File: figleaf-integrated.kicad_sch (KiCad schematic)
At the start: 63 parts, among them J1 UDB, J2 HRO_TYPE-C-31-M-14, J3 Battery, J9 TC2030_SWD, Q2 2N7002, SW1 PWR, SW2 RST, U1 SRV05-4, U10 MAX17048, U3 BQ24075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

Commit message: progress + add jst conn
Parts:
- J3: footprint PCM_marbastlib-various:Molex_Pico-EZmate_78171-0002_1x02-1MP_P1.20mm_Vertical -> Connector_JST:JST_SH_SM02B-SRSS-TB_1x02-1MP_P1.00mm_Horizontal
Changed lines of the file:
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@@
 			)
 		)
-		(property "Footprint" "PCM_marbastlib-various:Molex_Pico-EZmate_78171-0002_1x02-1MP_P1.20mm_Vertical"
+		(property "Footprint" "Connector_JST:JST_SH_SM02B-SRSS-TB_1x02-1MP_P1.00mm_Horizontal"
 			(at 236.22 57.15 0)
 			(effects

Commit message: Add matrix
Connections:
- net col_5: now also U8.11 (P0.27); no longer U8.35 (P1.10-LF)
- net row_0: now also U8.16 (P0.08); no longer U8.36 (P1.11-LF)
- net row_1: now also U8.15 (P0.11); no longer U8.37 (P1.12-LF)
- net row_2: now also U8.14 (P0.06); no longer U8.38 (P1.13-LF)
- net row_3: now also U8.13 (P0.04-A); no longer U8.40 (P1.14-LF)
- net row_4: now also U8.12 (P0.26); no longer U8.41 (P1.15-LF)

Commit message: tracing progress
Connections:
- net GNDPWR is gone; now on net GND_L: R1.1, R2.1
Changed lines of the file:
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@@
 	)
 	(symbol
-		(lib_id "power:GNDPWR")
+		(lib_id "power:GND")
 		(at 67.31 41.91 0)
 		(unit 1)
@@
 			)
 		)
-		(property "Value" "GNDPWR"
+		(property "Value" "GND_L"
 			(at 67.4116 45.8216 0)
 			(effects
@@
 		)
 		(property "Footprint" ""
-			(at 67.31 43.18 0)
+			(at 67.31 41.91 0)
 			(effects
 				(font
@@
 		)
 		(property "Datasheet" ""
-			(at 67.31 43.18 0)
+			(at 67.31 41.91 0)
 			(effects
 				(font
@@
 			)
 		)
-		(property "Description" "Power symbol creates a global label with name \"GNDPWR\" , global ground"
+		(property "Description" "Power symbol creates a global label with name \"GND\" , ground"
 			(at 67.31 41.91 0)
 			(effects

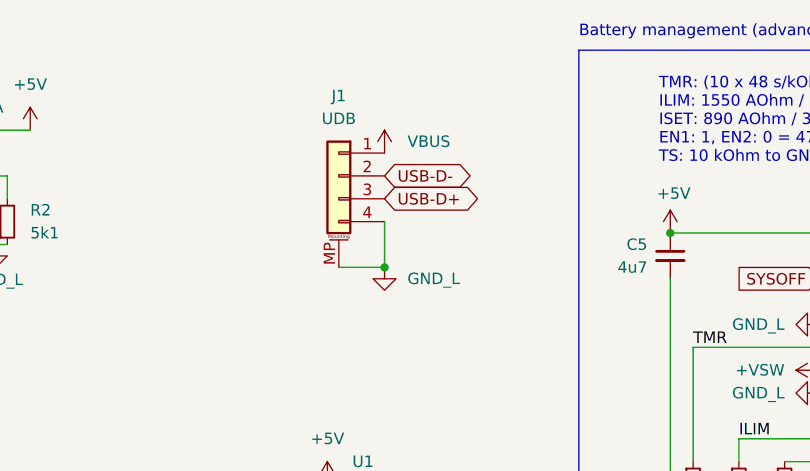
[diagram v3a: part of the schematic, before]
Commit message: remove J4 connector, not using DB board
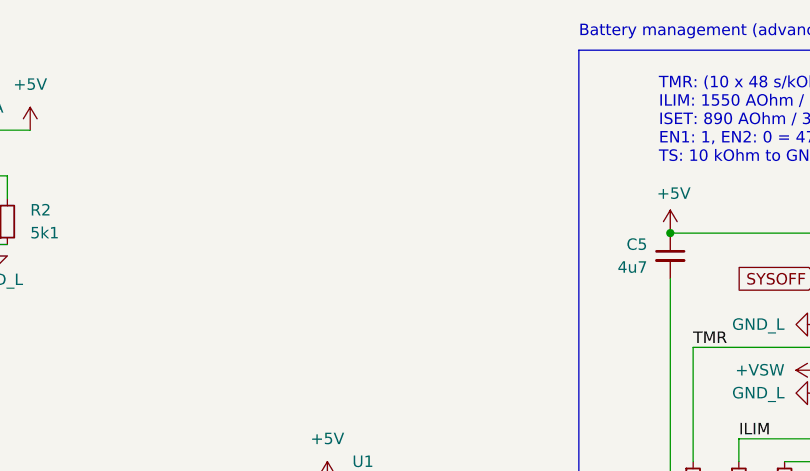
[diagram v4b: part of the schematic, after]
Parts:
- removed J1: UDB, symbol Connector_Generic_MountingPin:Conn_01x04_MountingPin

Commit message: pcb progress
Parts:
- U10: footprint Package_DFN_QFN:DFN-8-1EP_2x2mm_P0.5mm_EP0.7x1.3mm -> Graz_Footprints:DFN-8-1EP_2x2mm_P0.5mm_EP0.7x1.3mm
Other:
- moved on the sheet: U1
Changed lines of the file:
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@@
 	)
 	(no_connect
-		(at 116.84 78.74)
+		(at 116.84 43.18)
 	)
 	(no_connect
@@
 	)
 	(no_connect
-		(at 91.44 83.82)
+		(at 91.44 48.26)
 	)
 	(no_connect
@@
 	(global_label "USB-D-"
 		(shape bidirectional)
-		(at 91.44 78.74 180)
+		(at 91.44 43.18 180)
 		(fields_autoplaced yes)
 		(effects
@@
 		)
 		(property "Intersheetrefs" "${INTERSHEET_REFS}"
-			(at 79.1981 78.74 0)
+			(at 79.1981 43.18 0)
 			(effects
 				(font
@@
 	(global_label "USB-D+"
 		(shape bidirectional)
-		(at 116.84 83.82 0)
+		(at 116.84 48.26 0)
 		(fields_autoplaced yes)
 		(effects
@@
 		)
 		(property "Intersheetrefs" "${INTERSHEET_REFS}"
-			(at 129.0819 83.82 0)
+			(at 129.0819 48.26 0)
 			(effects
 				(font
@@
 	(symbol
 		(lib_id "power:GND")
-		(at 104.14 93.98 0)
+		(at 104.14 58.42 0)
 		(unit 1)
 		(exclude_from_sim no)
@@
 		(dnp no)
 		(property "Reference" "#PWR09"
-			(at 104.14 100.33 0)
+			(at 104.14 64.77 0)
 			(effects
 				(font
@@
 		)
 		(property "Value" "GND_L"
-			(at 104.267 98.3742 0)
+			(at 104.267 62.8142 0)
 			(effects
 				(font
@@
 		)
 		(property "Footprint" ""
-			(at 104.14 93.98 0)
+			(at 104.14 58.42 0)
 			(effects
 				(font
@@
 		)
 		(property "Datasheet" ""
-			(at 104.14 93.98 0)
+			(at 104.14 58.42 0)
 			(effects
 				(font
@@
 		)
 		(property "Description" "Power symbol creates a global label with name \"GND\" , ground"
-			(at 104.14 93.98 0)
+			(at 104.14 58.42 0)
 			(effects
 				(font
@@
 			)
 		)
-		(property "Footprint" "Package_DFN_QFN:DFN-8-1EP_2x2mm_P0.5mm_EP0.7x1.3mm"
+		(property "Footprint" "Graz_Footprints:DFN-8-1EP_2x2mm_P0.5mm_EP0.7x1.3mm"
 			(at 153.035 138.43 0)
 			(effects
@@
 	(symbol
 		(lib_id "Power_Protection:SRV05-4")
-		(at 104.14 81.28 0)
+		(at 104.14 45.72 0)
 		(unit 1)
 		(exclude_from_sim no)
@@
 		(fields_autoplaced yes)
 		(property "Reference" "U1"
-			(at 106.9087 66.04 0)
+			(at 106.9087 30.48 0)
 			(effects
 				(font
@@
 		)
 		(property "Value" "SRV05-4"
-			(at 106.9087 68.58 0)
+			(at 106.9087 33.02 0)
 			(effects
 				(font
@@
 		)
 		(property "Footprint" "Package_TO_SOT_SMD:SOT-23-6"
-			(at 121.92 92.71 0)
+			(at 121.92 57.15 0)
 			(effects
 				(font
@@
 		)
 		(property "Datasheet" "http://www.onsemi.com/pub/Collateral/SRV05-4-D.PDF"
-			(at 104.14 81.28 0)
+			(at 104.14 45.72 0)
 			(effects
 				(font
@@
 		)
 		(property "Description" "ESD Protection Diodes with Low Clamping Voltage, SOT-23-6"
-			(at 104.14 81.28 0)
+			(at 104.14 45.72 0)
 			(effects
 				(font
@@
 	(symbol
 		(lib_id "power:+5V")
-		(at 104.14 68.58 0)
+		(at 104.14 33.02 0)
 		(unit 1)
 		(exclude_from_sim no)
@@
 		(fields_autoplaced yes)
 		(property "Reference" "#PWR06"
-			(at 104.14 72.39 0)
+			(at 104.14 36.83 0)
 			(effects
 				(font
@@
 		)
 		(property "Value" "+5V"
-			(at 104.14 63.5 0)
+			(at 104.14 27.94 0)
 			(effects
 				(font
@@
 		)
 		(property "Footprint" ""
-			(at 104.14 68.58 0)
+			(at 104.14 33.02 0)
 			(effects
 				(font
@@
 		)
 		(property "Datasheet" ""
-			(at 104.14 68.58 0)
+			(at 104.14 33.02 0)
 			(effects
 				(font
@@
 		)
 		(property "Description" "Power symbol creates a global label with name \"+5V\""
-			(at 104.14 68.58 0)
+			(at 104.14 33.02 0)
 			(effects
 				(font

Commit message: move usb outwards + add mounting holes + fillet
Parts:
- added H1, H2, H3, H4, H5, H6, H7, H8: MountingHole, Graz_Footprints:m1.6, symbol Mechanical:MountingHole
